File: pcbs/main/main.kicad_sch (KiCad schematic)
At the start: 1 part

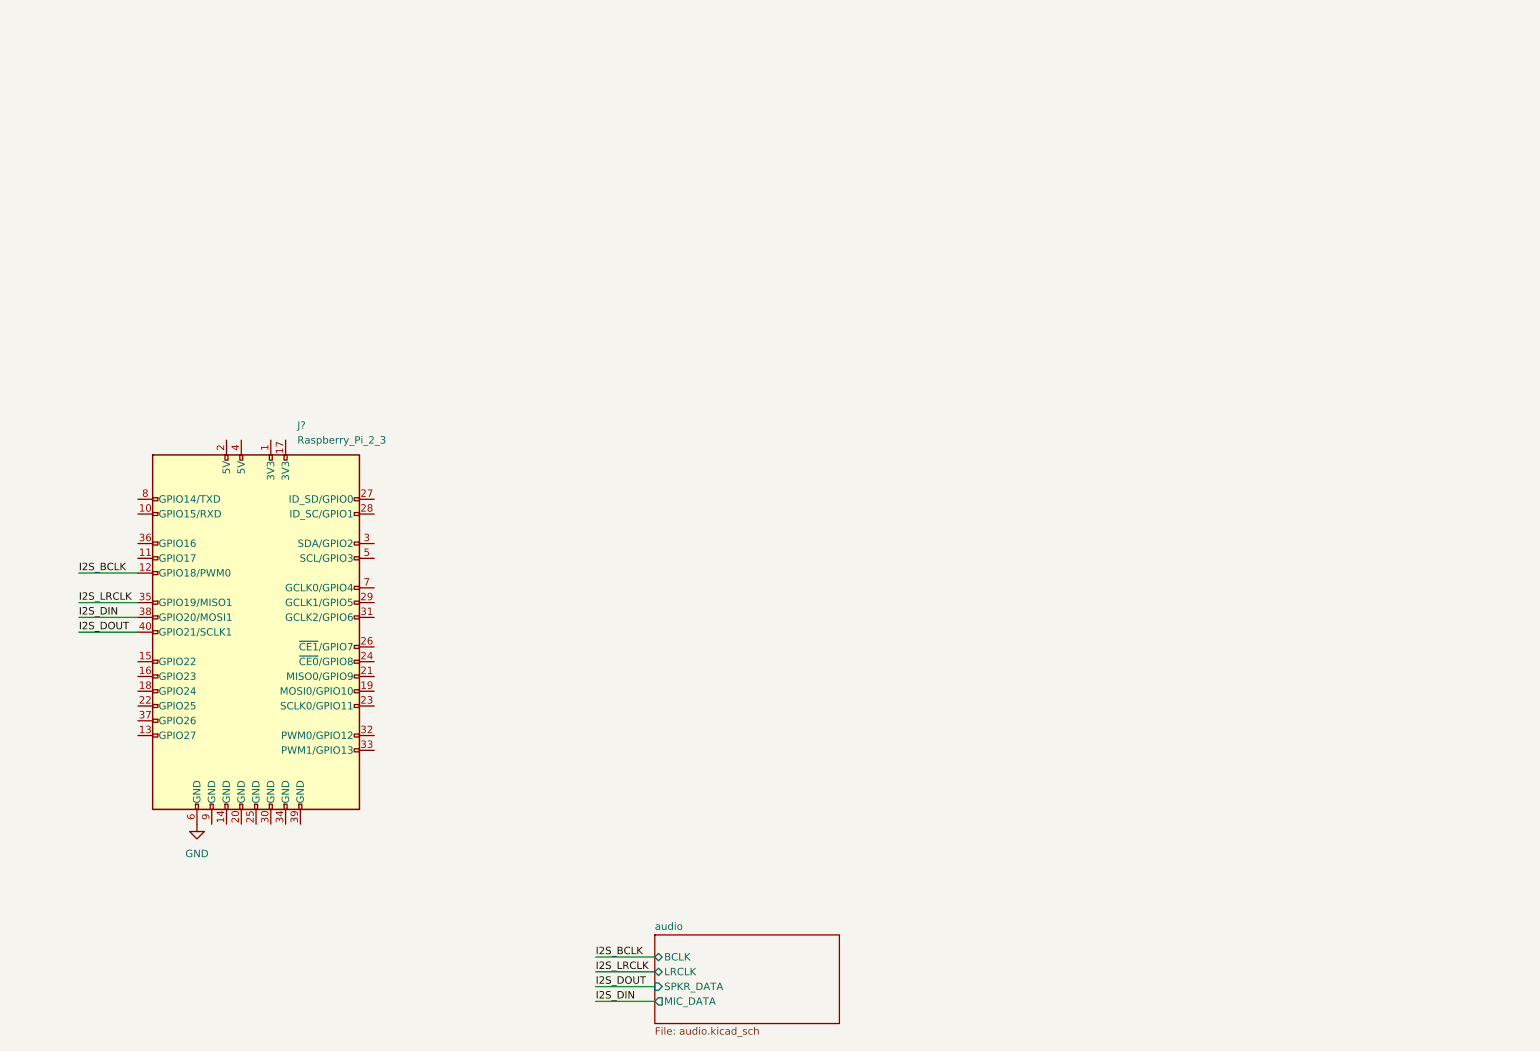
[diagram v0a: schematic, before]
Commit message: Add power input stage, add EEPROM for GPIO autoconfiguration.
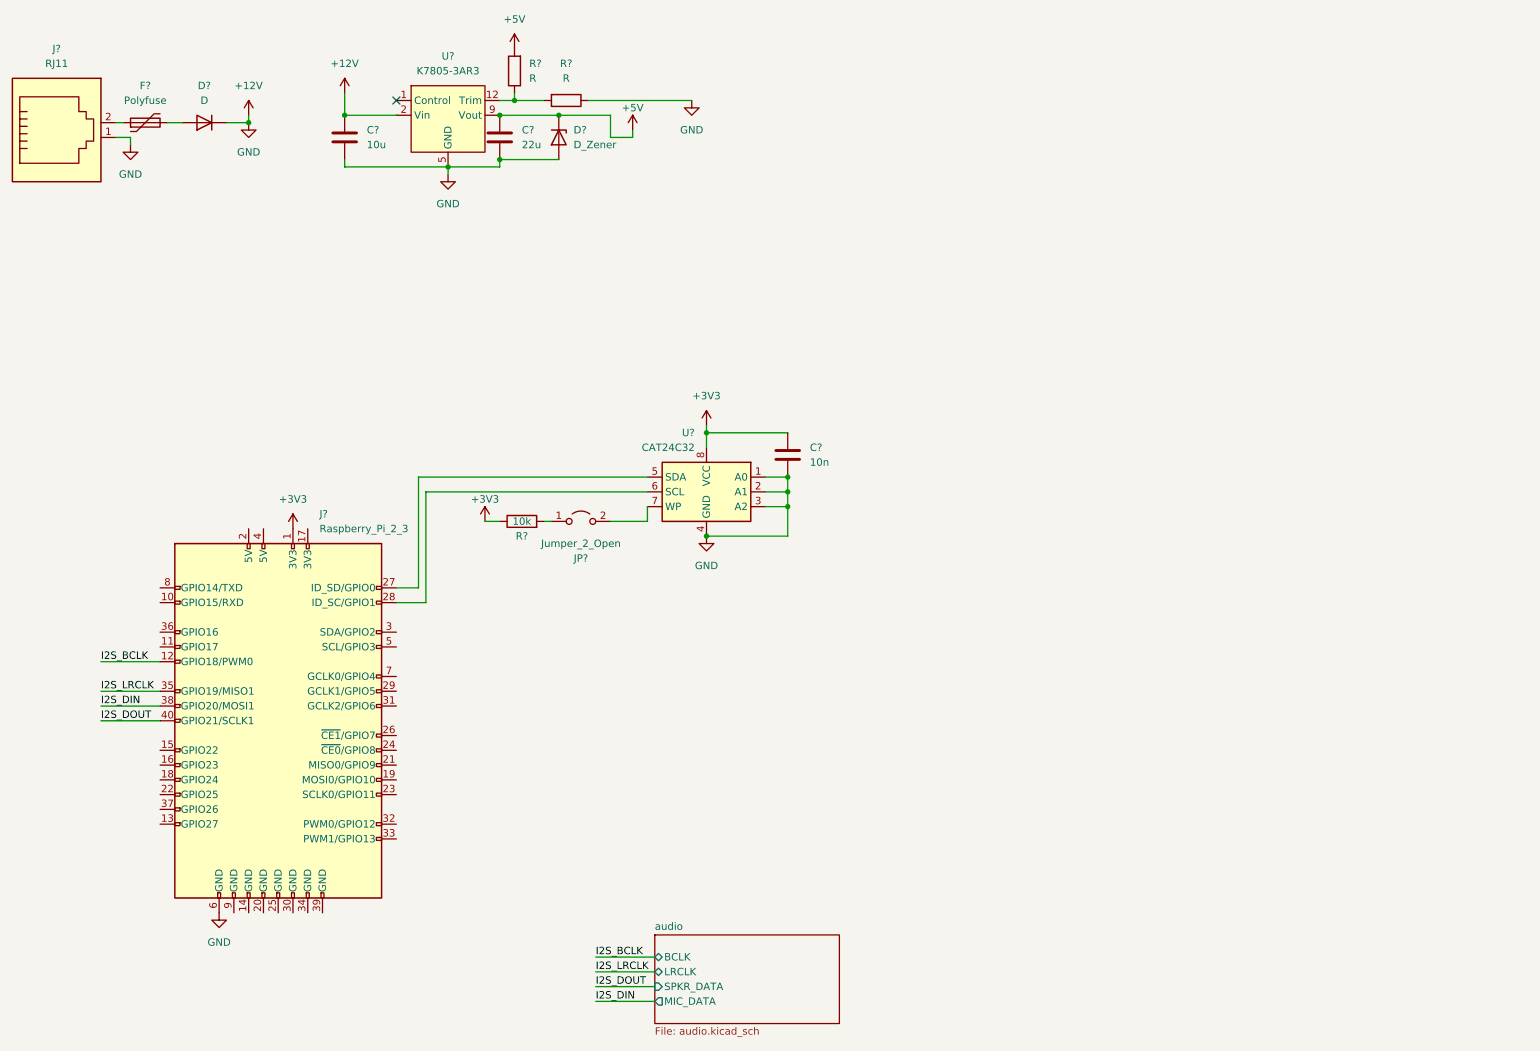
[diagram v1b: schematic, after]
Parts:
- added C?: 10n, symbol Device:C
- added C?: 10u, symbol Device:C
- added C?: 22u, symbol Device:C
- added D?: D, symbol Device:D
- added D?: D_Zener, symbol Device:D_Zener
- added F?: Polyfuse, symbol Device:Polyfuse
- added J?: RJ11, symbol Connector:RJ11
- added JP?: Jumper_2_Open, symbol Jumper:Jumper_2_Open
- added R?: 10k, symbol Device:R
- added R? (x2): R, symbol Device:R
- added U?: CAT24C32, symbol Memory_EEPROM:CAT24C128
- added U?: K7805-3AR3, symbol pividbell_main_parts:K7805-3AR3
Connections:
- net +3V3: now reaches J?.1 (3V3)
- net +3V3: now also C?.1, R?.1, U?.8 (VCC)
- net at J?.27 (ID_SD/GPIO0): now also U?.5 (SDA)
- net at J?.28 (ID_SC/GPIO1): now also U?.6 (SCL)
- net GND renamed +12V
- net +12V: now also C?.1, C?.2, C?.2, C?.2, D?.1 (K), D?.2 (A), J?.1, R?.1, U?.1 (A0), U?.2 (A1), U?.2 (Vin), U?.3 (A2), U?.3 (Vin), U?.4 (GND), U?.4 (Vin), U?.5 (GND), U?.6 (GND), U?.7 (GND), U?.8 (GND)
- new net: D?.2 (A), F?.2
- new net: JP?.2 (B), U?.7 (WP)
- new net: JP?.1 (A), R?.2
- new net: R?.1, R?.2, U?.12 (Trim)
- new net: F?.1, J?.2
- new net +5V: C?.1, D?.1 (K), R?.2, U?.10 (Vout), U?.11 (Vout), U?.9 (Vout)
- no-connect marks 0 -> 1
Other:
- moved on the sheet: J?

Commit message: Add microphone ADC
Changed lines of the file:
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@@
     (stroke (width 0) (type default) (color 0 0 0 0))
   )
-  (wire (pts (xy 124.46 179.07) (xy 134.62 179.07))
+  (wire (pts (xy 113.03 170.18) (xy 123.19 170.18))
     (stroke (width 0) (type default) (color 0 0 0 0))
   )
@@
     (stroke (width 0) (type default) (color 0 0 0 0))
   )
-  (wire (pts (xy 124.46 176.53) (xy 134.62 176.53))
+  (wire (pts (xy 113.03 167.64) (xy 123.19 167.64))
     (stroke (width 0) (type default) (color 0 0 0 0))
   )
@@
     (stroke (width 0) (type default) (color 0 0 0 0))
   )
-  (wire (pts (xy 124.46 181.61) (xy 134.62 181.61))
+  (wire (pts (xy 113.03 172.72) (xy 123.19 172.72))
     (stroke (width 0) (type default) (color 0 0 0 0))
   )
@@
     (stroke (width 0) (type default) (color 0 0 0 0))
   )
-  (wire (pts (xy 124.46 184.15) (xy 134.62 184.15))
+  (wire (pts (xy 113.03 175.26) (xy 123.19 175.26))
     (stroke (width 0) (type default) (color 0 0 0 0))
   )
@@
     (effects (font (size 1.27 1.27)) (justify left bottom))
   )
-  (label "I2S_DIN" (at 124.46 184.15 0)
+  (label "I2S_DIN" (at 113.03 175.26 0)
     (effects (font (size 1.27 1.27)) (justify left bottom))
   )
@@
     (effects (font (size 1.27 1.27)) (justify left bottom))
   )
-  (label "I2S_BCLK" (at 124.46 176.53 0)
+  (label "I2S_BCLK" (at 113.03 167.64 0)
     (effects (font (size 1.27 1.27)) (justify left bottom))
   )
-  (label "I2S_LRCLK" (at 124.46 179.07 0)
+  (label "I2S_LRCLK" (at 113.03 170.18 0)
     (effects (font (size 1.27 1.27)) (justify left bottom))
   )
-  (label "I2S_DOUT" (at 124.46 181.61 0)
+  (label "I2S_DOUT" (at 113.03 172.72 0)
     (effects (font (size 1.27 1.27)) (justify left bottom))
   )
@@
     (pin "2")
   )
-  (sheet (at 134.62 172.72) (size 31.75 15.24) (fields_autoplaced)
+  (sheet (at 123.19 163.83) (size 31.75 15.24) (fields_autoplaced)
     (stroke (width 0.1524) (type solid) (color 0 0 0 0))
     (fill (color 0 0 0 0.0000))
-    (property "Sheet name" "audio" (id 0) (at 134.62 172.0084 0)
+    (property "Sheet name" "audio" (id 0) (at 123.19 163.1184 0)
       (effects (font (size 1.27 1.27)) (justify left bottom))
     )
-    (property "Sheet file" "audio.kicad_sch" (id 1) (at 134.62 188.5446 0)
+    (property "Sheet file" "audio.kicad_sch" (id 1) (at 123.19 179.6546 0)
       (effects (font (size 1.27 1.27)) (justify left top))
     )
-    (pin "MIC_DATA" output (at 134.62 184.15 180)
-      (effects (font (size 1.27 1.27)) (justify left))
-    )
-    (pin "BCLK" bidirectional (at 134.62 176.53 180)
-      (effects (font (size 1.27 1.27)) (justify left))
-    )
-    (pin "SPKR_DATA" input (at 134.62 181.61 180)
-      (effects (font (size 1.27 1.27)) (justify left))
-    )
-    (pin "LRCLK" bidirectional (at 134.62 179.07 180)
+    (pin "MIC_DATA" output (at 123.19 175.26 180)
+      (effects (font (size 1.27 1.27)) (justify left))
+    )
+    (pin "BCLK" bidirectional (at 123.19 167.64 180)
+      (effects (font (size 1.27 1.27)) (justify left))
+    )
+    (pin "SPKR_DATA" input (at 123.19 172.72 180)
+      (effects (font (size 1.27 1.27)) (justify left))
+    )
+    (pin "LRCLK" bidirectional (at 123.19 170.18 180)
       (effects (font (size 1.27 1.27)) (justify left))
     )
@@
       (reference "#PWR?") (unit 1) (value "GND") (footprint "")
     )
+    (path "/c9bcbb20-bce5-48eb-aaa8-469331798139/46cc0fd6-5127-4541-8cbd-16b3c454ec30"
+      (reference "#PWR?") (unit 1) (value "+3V3") (footprint "")
+    )
+    (path "/c9bcbb20-bce5-48eb-aaa8-469331798139/49c576fb-36cc-457c-913f-64856c713747"
+      (reference "#PWR?") (unit 1) (value "GND") (footprint "")
+    )
+    (path "/c9bcbb20-bce5-48eb-aaa8-469331798139/51180f80-2e38-4b4b-bcae-d935a452b9ac"
+      (reference "#PWR?") (unit 1) (value "GND") (footprint "")
+    )
     (path "/5a3e5c1e-d818-454f-996c-fc29d038aef8"
       (reference "#PWR?") (unit 1) (value "+3V3") (footprint "")
@@
     )
     (path "/60e34a1e-e74b-4478-a63b-76a18bae9efe"
+      (reference "#PWR?") (unit 1) (value "GND") (footprint "")
+    )
+    (path "/c9bcbb20-bce5-48eb-aaa8-469331798139/66e41d15-58fe-421c-879c-5a5ec35cc159"
+      (reference "#PWR?") (unit 1) (value "GND") (footprint "")
+    )
+    (path "/c9bcbb20-bce5-48eb-aaa8-469331798139/73507f45-6922-46a3-97fd-24e7efed8d39"
+      (reference "#PWR?") (unit 1) (value "GND") (footprint "")
+    )
+    (path "/c9bcbb20-bce5-48eb-aaa8-469331798139/7c325a6b-c170-4c02-9aea-34e929f042b3"
       (reference "#PWR?") (unit 1) (value "GND") (footprint "")
     )
@@
       (reference "#PWR?") (unit 1) (value "+3V3") (footprint "")
     )
+    (path "/c9bcbb20-bce5-48eb-aaa8-469331798139/e8bcc4b4-c48e-4987-a93f-f4bd0390d3d4"
+      (reference "#PWR?") (unit 1) (value "GND") (footprint "")
+    )
+    (path "/c9bcbb20-bce5-48eb-aaa8-469331798139/eaa9c740-0990-484c-9f57-70927834192b"
+      (reference "#PWR?") (unit 1) (value "+3V3") (footprint "")
+    )
+    (path "/c9bcbb20-bce5-48eb-aaa8-469331798139/eda44fcb-6711-4f46-a108-b2fd9ef9a41d"
+      (reference "#PWR?") (unit 1) (value "+3V3") (footprint "")
+    )
+    (path "/c9bcbb20-bce5-48eb-aaa8-469331798139/fe60cf0c-f0d7-41ae-8957-bf23b0dc3dec"
+      (reference "#PWR?") (unit 1) (value "GND") (footprint "")
+    )
     (path "/09a2e506-7b9e-4939-b88b-3d561d5c8ab0"
       (reference "C?") (unit 1) (value "10n") (footprint "")
@@
       (reference "C?") (unit 1) (value "10u") (footprint "")
     )
+    (path "/c9bcbb20-bce5-48eb-aaa8-469331798139/1740d004-8130-497a-b9db-37a01a9a22ca"
+      (reference "C?") (unit 1) (value "10u") (footprint "")
+    )
     (path "/c9bcbb20-bce5-48eb-aaa8-469331798139/2fecbd38-48ed-441e-8503-3637d2228528"
       (reference "C?") (unit 1) (value "220u") (footprint "")
     )
+    (path "/c9bcbb20-bce5-48eb-aaa8-469331798139/37c30413-4384-47d2-a5e4-0116e2e37447"
+      (reference "C?") (unit 1) (value "10u") (footprint "")
+    )
     (path "/c9bcbb20-bce5-48eb-aaa8-469331798139/4be6c124-ae67-4a93-92c3-f5ebb66896d2"
       (reference "C?") (unit 1) (value "10u") (footprint "")
@@
       (reference "C?") (unit 1) (value "0.05u") (footprint "")
     )
+    (path "/c9bcbb20-bce5-48eb-aaa8-469331798139/5d70e13c-3030-4e6c-83a4-db0b7b040848"
+      (reference "C?") (unit 1) (value "0.1u") (footprint "")
+    )
+    (path "/c9bcbb20-bce5-48eb-aaa8-469331798139/6693416e-c218-4225-bf8c-203de3184cc6"
+      (reference "C?") (unit 1) (value "0.1u") (footprint "")
+    )
     (path "/c9bcbb20-bce5-48eb-aaa8-469331798139/6d17e313-32c7-43d0-b4c7-349c774d30c7"
       (reference "C?") (unit 1) (value "2.2n") (footprint "")
     )
+    (path "/c9bcbb20-bce5-48eb-aaa8-469331798139/83b9a4f1-f335-4bc2-9cad-cc27bdf156a7"
+      (reference "C?") (unit 1) (value "2.2u") (footprint "")
+    )
     (path "/c9bcbb20-bce5-48eb-aaa8-469331798139/8d8d8faf-6c60-404a-ab82-3bfacff52694"
       (reference "C?") (unit 1) (value "0.1u") (footprint "")
@@
       (reference "C?") (unit 1) (value "2.2u") (footprint "")
     )
+    (path "/c9bcbb20-bce5-48eb-aaa8-469331798139/a3942f56-db20-4420-a986-eb6c91fb6e06"
+      (reference "C?") (unit 1) (value "0.1u") (footprint "")
+    )
     (path "/c9bcbb20-bce5-48eb-aaa8-469331798139/b5d0444e-9218-4252-8254-6ae7f6e3ab2b"
       (reference "C?") (unit 1) (value "10u") (footprint "")
     )
+    (path "/c9bcbb20-bce5-48eb-aaa8-469331798139/b788ad77-918e-4172-89e1-a03585ef8812"
+      (reference "C?") (unit 1) (value "0.1u") (footprint "")
+    )
     (path "/c9bcbb20-bce5-48eb-aaa8-469331798139/ba7673e9-d14c-42cd-b620-ecb3145f737a"
+      (reference "C?") (unit 1) (value "10u") (footprint "")
+    )
+    (path "/c9bcbb20-bce5-48eb-aaa8-469331798139/bebccbaf-f974-4003-b23e-0cb0ed3ca32a"
       (reference "C?") (unit 1) (value "10u") (footprint "")
     )
@@
       (reference "C?") (unit 1) (value "100u") (footprint "")
     )
+    (path "/c9bcbb20-bce5-48eb-aaa8-469331798139/f37ff452-6805-4d29-95dc-80fe3ff7b009"
+      (reference "C?") (unit 1) (value "10u") (footprint "")
+    )
     (path "/c9bcbb20-bce5-48eb-aaa8-469331798139/f4736beb-955e-45d9-bb04-c50f6218e7c1"
       (reference "C?") (unit 1) (value "2.2u") (footprint "")
     )
+    (path "/c9bcbb20-bce5-48eb-aaa8-469331798139/f8d60052-1827-4f0b-b9d5-716c323a0d62"
+      (reference "C?") (unit 1) (value "10u") (footprint "")
+    )
     (path "/c9bcbb20-bce5-48eb-aaa8-469331798139/fac9f493-6f0a-4587-9630-d6aa4c9b4397"
       (reference "C?") (unit 1) (value "100u") (footprint "")
@@
       (reference "LS?") (unit 1) (value "Speaker") (footprint "")
     )
+    (path "/c9bcbb20-bce5-48eb-aaa8-469331798139/f6a63bdb-a497-4bdc-b614-039d74749a43"
+      (reference "MK?") (unit 1) (value "Microphone") (footprint "")
+    )
     (path "/c9bcbb20-bce5-48eb-aaa8-469331798139/165ee7e1-b0f3-41a6-818b-678b0c672594"
       (reference "R?") (unit 1) (value "10k") (footprint "")
@@
       (reference "R?") (unit 1) (value "R") (footprint "")
     )
+    (path "/c9bcbb20-bce5-48eb-aaa8-469331798139/f8ee2805-625c-4280-b190-8aec0c73cf9b"
+      (reference "R?") (unit 1) (value "2k2") (footprint "")
+    )
     (path "/c9bcbb20-bce5-48eb-aaa8-469331798139/0c820c07-8709-47be-8e45-880d1b3be58e"
       (reference "U?") (unit 1) (value "LM386N-4") (footprint "")
@@
       (reference "U?") (unit 1) (value "CAT24C32") (footprint "")
     )
-    (path "/c9bcbb20-bce5-48eb-aaa8-469331798139/15d0d989-c057-47ce-a42b-bc0875b50f04"
-      (reference "U?") (unit 1) (value "AK5720VT") (footprint "Package_SO:TSSOP-16_4.4x5mm_P0.65mm")
+    (path "/c9bcbb20-bce5-48eb-aaa8-469331798139/8e331940-2b25-4cb2-b301-bce402d550e1"
+      (reference "U?") (unit 1) (value "PCM1860") (footprint "")
     )
     (path "/a4557600-a8ae-411b-b0f5-d7b885f9c0f1"
